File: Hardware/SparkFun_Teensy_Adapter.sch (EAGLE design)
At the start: 7 parts, among them J1 ARDUINO_R3_SHIELD, J2 AVR_SPI_PRG_6PTH

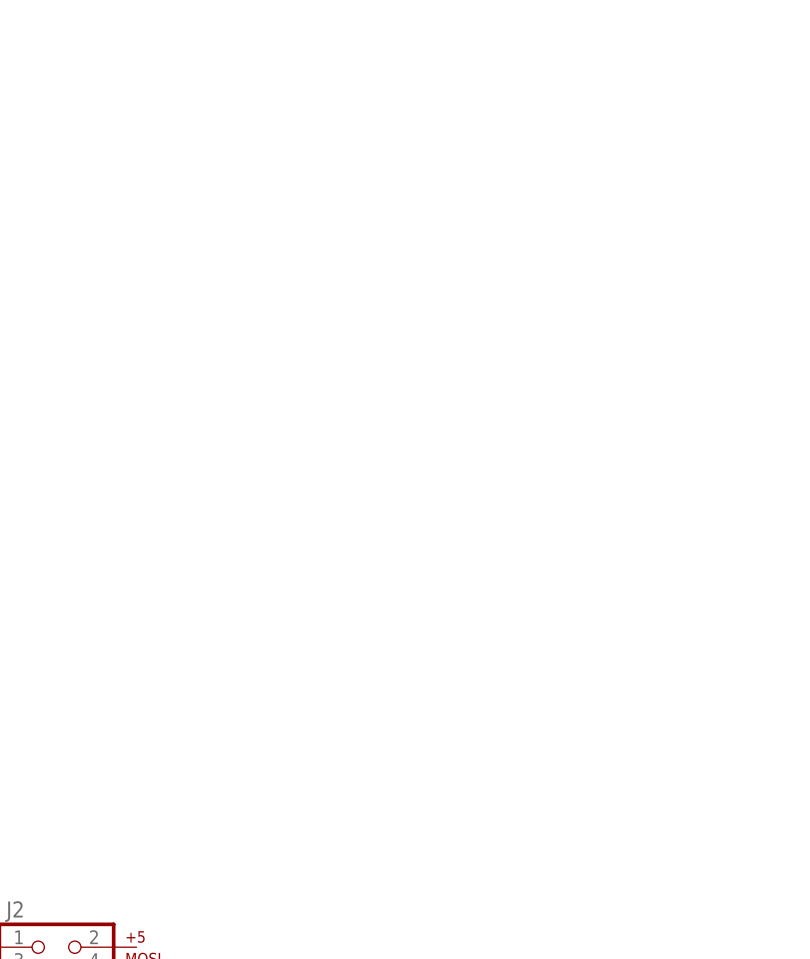
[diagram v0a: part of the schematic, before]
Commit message: Basic mechanical layout of board.
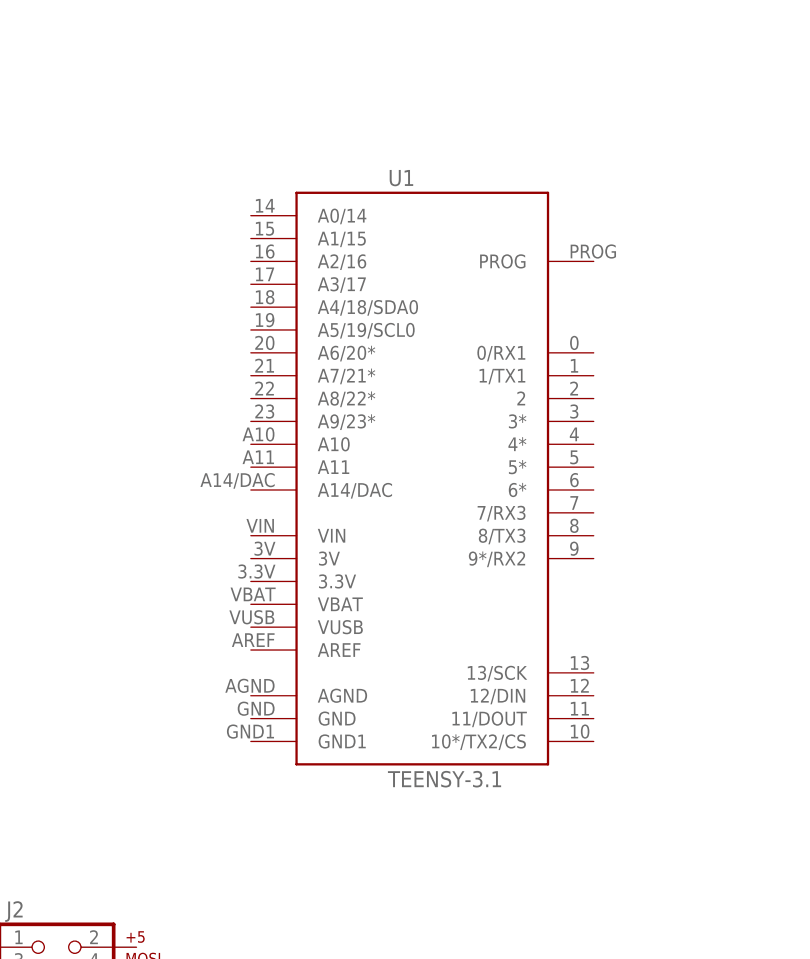
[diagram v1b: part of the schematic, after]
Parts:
- added U1: TEENSY-3.1, Testing:TEENSY-3.1
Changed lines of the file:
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@@
 <layer number="251" name="SMDround" color="12" fill="11" visible="no" active="no"/>
 <layer number="254" name="cooling" color="7" fill="1" visible="yes" active="yes"/>
+<layer number="255" name="routoute" color="7" fill="1" visible="yes" active="yes"/>
 </layers>
 <schematic xreflabel="%F%N/%S" xrefpart="/%S.%C%R">
@@
 <part name="J1" library="SparkFun-Boards" deviceset="ARDUINO_R3_SHIELD" device=""/>
 <part name="J2" library="SparkFun-Connectors" deviceset="AVR_SPI_PRG_6" device="PTH"/>
+<part name="U1" library="Testing" deviceset="TEENSY-3.1" device=""/>
 </parts>
 <sheets>
@@
 <instance part="J1" gate="G$1" x="88.9" y="109.22"/>
 <instance part="J2" gate="G$1" x="127" y="66.04"/>
+<instance part="U1" gate="G$1" x="154.94" y="88.9"/>
 </instances>
 <busses>

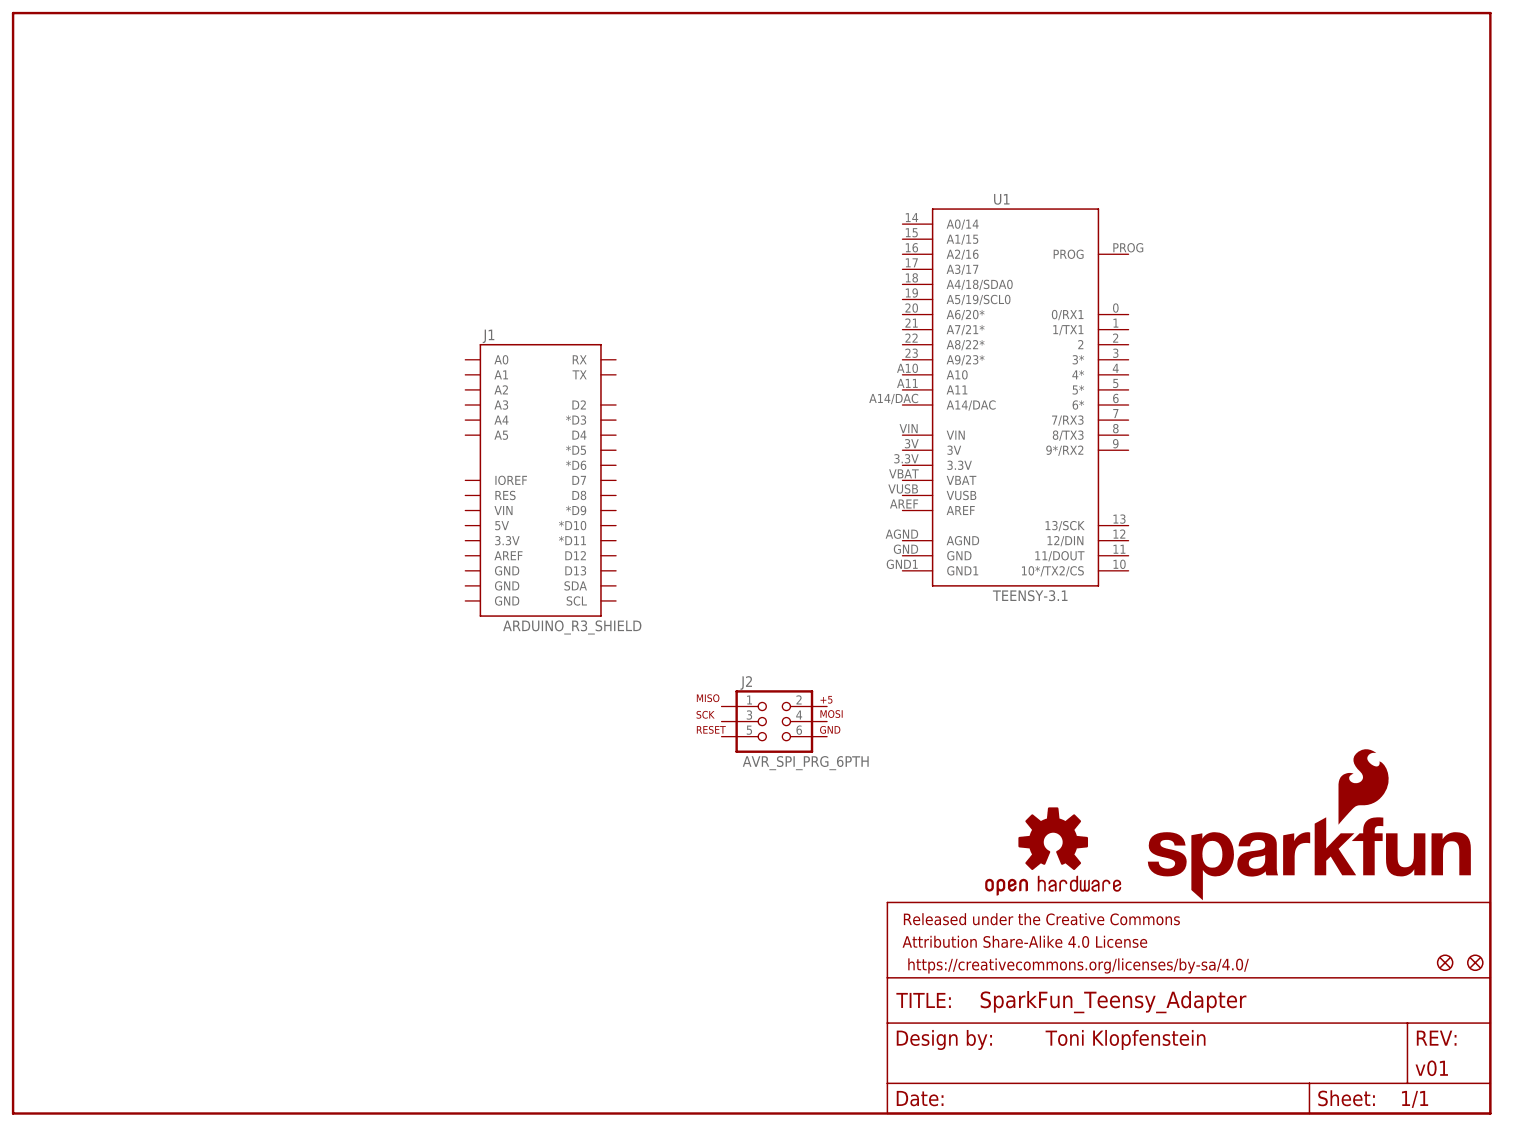
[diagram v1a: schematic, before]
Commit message: Power connectors added
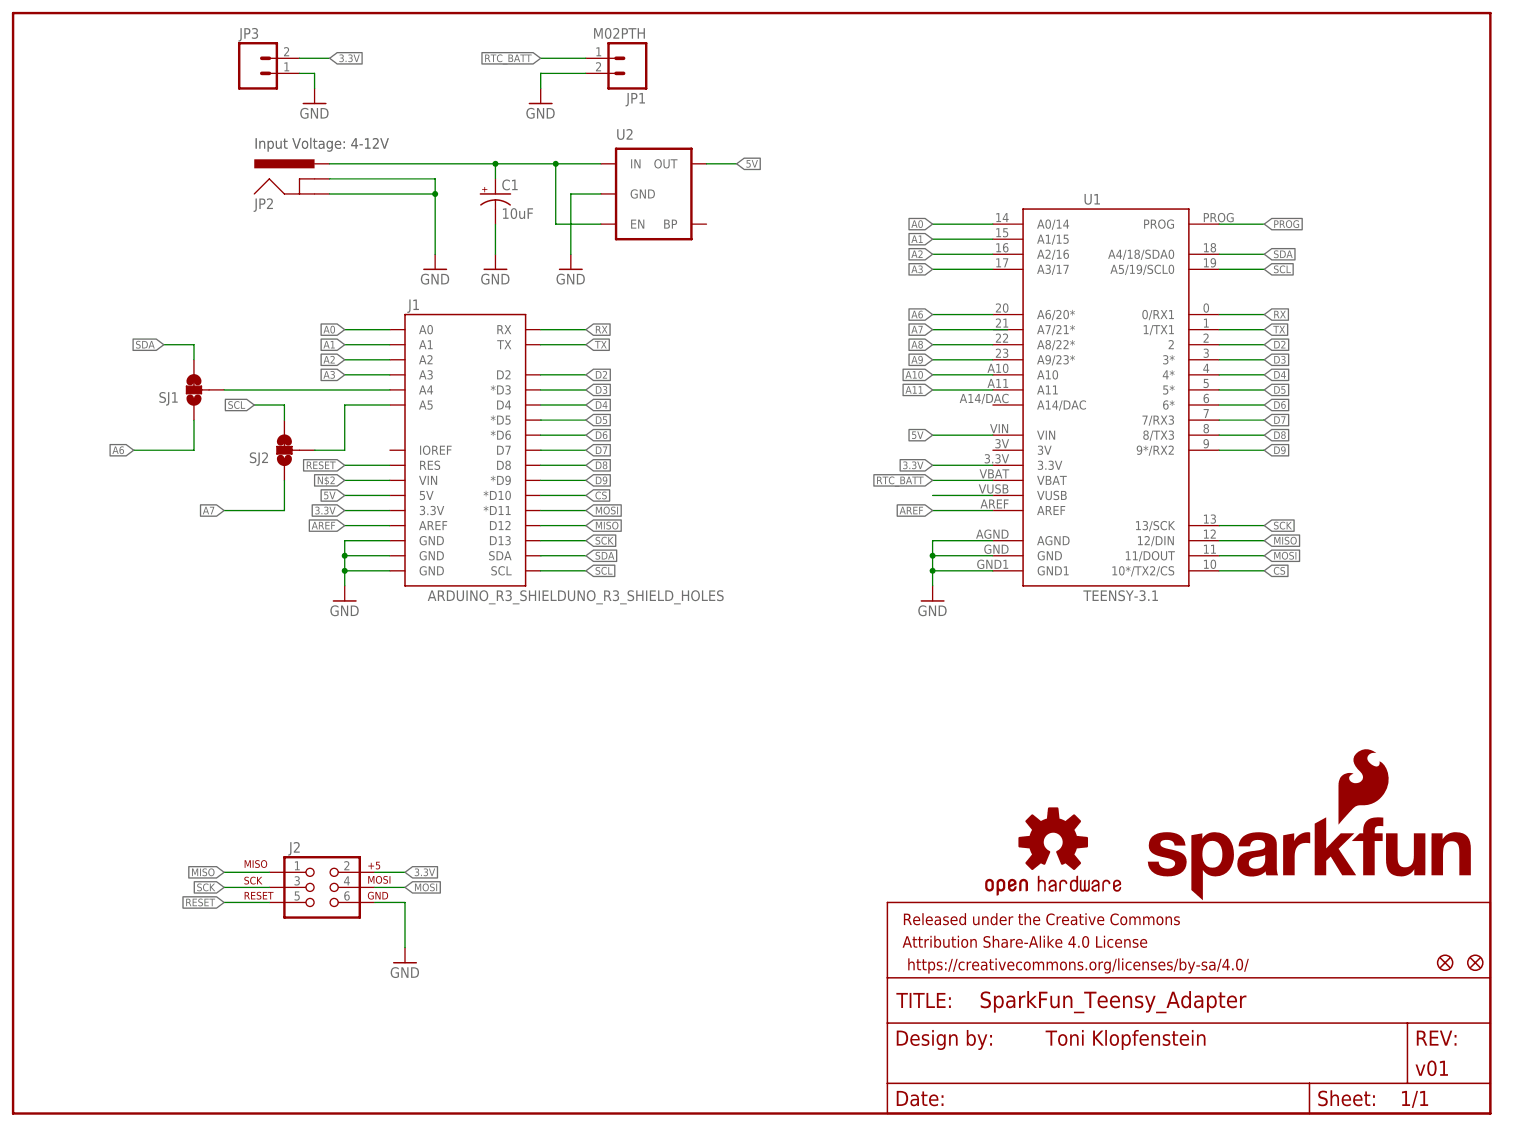
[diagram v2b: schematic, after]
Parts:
- added C1: 10uF, SparkFun-Capacitors:10UF-16V-10%(TANT)
- added JP1: M02PTH, SparkFun-Connectors:M02PTH
- added JP2: POWER_JACKPTH_LOCK, SparkFun-Connectors:POWER_JACKPTH_LOCK
- added JP3: M02JST-PTH-2, SparkFun-Connectors:M02JST-PTH-2
- added SJ1, SJ2: JUMPER-PAD-3-2OF3_NC_BY_TRACE_SMALL, SparkFun-Passives:JUMPER-PAD-3-2OF3_NC_BY_TRACE_SMALL
- added U2: (no value), SparkFun-PowerIC:MIC52055V
- J1: value ARDUINO_R3_SHIELD -> ARDUINO_R3_SHIELDUNO_R3_SHIELD_HOLES; device SparkFun-Boards:ARDUINO_R3_SHIELD -> Testing:ARDUINO_R3_SHIELDUNO_R3_SHIELD_HOLES
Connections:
- new net 3.3V: J1.3.3V, J2.2, JP3.2, U1.3.3V
- new net 5V: J1.5V, U1.VIN, U2.OUT
- new net A0: J1.A0, U1.A0/14
- new net A1: J1.A1, U1.A1/15
- new net A10: U1.A10
- new net A11: U1.A11
- new net A2: J1.A2, U1.A2/16
- new net A3: J1.A3, U1.A3/17
- new net A4: J1.A4, SJ1.2
- new net A5: J1.A5, SJ2.2
- new net A6: SJ1.1, U1.A6/20*
- new net A7: SJ2.1
- new net A8: U1.A8/22*
- new net A9: U1.A9/23*
- new net AREF: J1.AREF, U1.AREF
- new net CS: J1.*D10, U1.10*/TX2/CS
- new net D2: J1.D2, U1.2
- new net D3: J1.*D3, U1.3*
- new net D4: J1.D4, U1.4*
- new net D5: J1.*D5, U1.5*
- new net D6: J1.*D6, U1.6*
- new net D7: J1.D7, U1.7/RX3
- new net D8: J1.D8, U1.8/TX3
- new net D9: J1.*D9, U1.9*/RX2
- new net GND: C1.-, J1.GND@0, J1.GND@1, J1.GND@2, J2.6, JP1.2, JP2.GND, JP2.GNDBREAK, JP3.1, U1.AGND, U1.GND, U1.GND1, U2.GND
- new net MISO: J1.D12, J2.1, U1.12/DIN
- new net MOSI: J1.*D11, J2.4, U1.11/DOUT
- new net N$2: J1.VIN
- new net N$6: U1.VUSB
- new net PROG: U1.PROG
- new net RESET: J1.RES, J2.5
- new net RTC_BATT: JP1.1, U1.VBAT
- new net RX: J1.RX, U1.0/RX1
- new net SCK: J1.D13, J2.3, U1.13/SCK
- new net SCL: J1.SCL, SJ2.3, U1.A5/19/SCL0
- new net SDA: J1.SDA, SJ1.3, U1.A4/18/SDA0
- new net TX: J1.TX, U1.1/TX1
- new net VRAW: C1.+, JP2.PWR, U2.EN, U2.IN
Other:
- note added: "Input Voltage: 4-12V"
- moved on the sheet: J1, J2, U1

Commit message: Partial routing
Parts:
- added C2: (no value), SparkFun-Capacitors:CAP_POL7343
- added JP4: (no value), SparkFun-Connectors:M08
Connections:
- removed net N$6: U1.VUSB
- new net A14/DAC: JP4.2, U1.A14/DAC
- new net HV_AREF: J1.AREF
- new net N$9: JP4.1
- new net VUSB: C2.+, JP4.7, U1.VUSB
- net A10: now also JP4.4
- net A11: now also JP4.3
- net A8: now also JP4.6
- net A9: now also JP4.5
- net AREF: no longer J1.AREF
- net GND: now also C2.-
- net PROG: now also JP4.8
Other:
- note added: "5V"
- note added: "Add 100uF Cap for USB Host applications."
- note added: "Add 32.768kHZ crystal to Teensy for use of RTC."
- note added: "Cut trace between VUSB and VIN pads on Teensy to use external power supply."
- note added: "DNP"
- moved on the sheet: JP1
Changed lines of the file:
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@@
 <part name="C1" library="SparkFun-Capacitors" deviceset="10UF-16V-10%(TANT)" device="" value="10uF"/>
 <part name="GND8" library="SparkFun-Aesthetics" deviceset="GND" device=""/>
+<part name="C2" library="SparkFun-Capacitors" deviceset="CAP_POL" device="7343"/>
+<part name="GND9" library="SparkFun-Aesthetics" deviceset="GND" device=""/>
+<part name="JP4" library="SparkFun-Connectors" deviceset="M08" device=""/>
 </parts>
 <sheets>
@@
 <plain>
 <text x="40.64" y="162.56" size="1.778" layer="97">Input Voltage: 4-12V</text>
+<text x="106.68" y="144.78" size="1.778" layer="97">5V</text>
+<text x="193.04" y="170.18" size="1.778" layer="97">DNP</text>
+<text x="200.66" y="172.72" size="1.27" layer="97">Add 100uF Cap for USB Host applications. </text>
+<text x="149.86" y="160.02" size="1.27" layer="97">Add 32.768kHZ crystal to Teensy for use of RTC.  </text>
+<text x="33.02" y="147.32" size="1.27" layer="97">Cut trace between VUSB and VIN pads
+ on Teensy to use external power supply. </text>
 </plain>
 <instances>
@@
 <attribute name="NAME" x="43.18" y="111.379" size="1.778" layer="95" rot="R180"/>
 </instance>
-<instance part="JP1" gate="G$1" x="104.14" y="177.8" rot="R180"/>
-<instance part="GND4" gate="1" x="88.9" y="170.18"/>
+<instance part="JP1" gate="G$1" x="172.72" y="175.26" rot="R180"/>
+<instance part="GND4" gate="1" x="160.02" y="165.1"/>
 <instance part="JP2" gate="G$1" x="50.8" y="152.4" smashed="yes">
 <attribute name="NAME" x="40.64" y="152.4" size="1.778" layer="95"/>
@@
 <instance part="C1" gate="G$1" x="81.28" y="154.94"/>
 <instance part="GND8" gate="1" x="81.28" y="142.24"/>
+<instance part="C2" gate="G$1" x="190.5" y="175.26"/>
+<instance part="GND9" gate="1" x="190.5" y="165.1"/>
+<instance part="JP4" gate="G$1" x="101.6" y="38.1"/>
 </instances>
 <busses>
@@
 <segment>
 <pinref part="JP1" gate="G$1" pin="2"/>
-<wire x1="96.52" y1="175.26" x2="88.9" y2="175.26" width="0.1524" layer="91"/>
-<wire x1="88.9" y1="175.26" x2="88.9" y2="172.72" width="0.1524" layer="91"/>
+<wire x1="165.1" y1="172.72" x2="160.02" y2="172.72" width="0.1524" layer="91"/>
+<wire x1="160.02" y1="172.72" x2="160.02" y2="167.64" width="0.1524" layer="91"/>
 <pinref part="GND4" gate="1" pin="GND"/>
 </segment>
@@
 <wire x1="81.28" y1="149.86" x2="81.28" y2="144.78" width="0.1524" layer="91"/>
 </segment>
+<segment>
+<pinref part="C2" gate="G$1" pin="-"/>
+<wire x1="190.5" y1="170.18" x2="190.5" y2="167.64" width="0.1524" layer="91"/>
+<pinref part="GND9" gate="1" pin="GND"/>
+</segment>
 </net>
 <net name="RX" class="0">
@@
 <label x="154.94" y="124.46" size="1.27" layer="95" rot="R180" xref="yes"/>
 </segment>
+<segment>
+<pinref part="JP4" gate="G$1" pin="4"/>
+<wire x1="106.68" y1="38.1" x2="114.3" y2="38.1" width="0.1524" layer="91"/>
+<label x="114.3" y="38.1" size="1.27" layer="95" xref="yes"/>
+</segment>
 </net>
 <net name="A11" class="0">
@@
 <wire x1="165.1" y1="121.92" x2="154.94" y2="121.92" width="0.1524" layer="91"/>
 <label x="154.94" y="121.92" size="1.27" layer="95" rot="R180" xref="yes"/>
+</segment>
+<segment>
+<pinref part="JP4" gate="G$1" pin="3"/>
+<wire x1="106.68" y1="35.56" x2="114.3" y2="35.56" width="0.1524" layer="91"/>
+<label x="114.3" y="35.56" size="1.27" layer="95" xref="yes"/>
 </segment>
 </net>
@@
 <net name="AREF" class="0">
 <segment>
-<pinref part="J1" gate="G$1" pin="AREF"/>
-<wire x1="63.5" y1="99.06" x2="55.88" y2="99.06" width="0.1524" layer="91"/>
-<label x="55.88" y="99.06" size="1.27" layer="95" rot="R180" xref="yes"/>
-</segment>
-<segment>
 <pinref part="U1" gate="G$1" pin="AREF"/>
 <wire x1="165.1" y1="101.6" x2="154.94" y2="101.6" width="0.1524" layer="91"/>
@@
 <segment>
 <pinref part="JP1" gate="G$1" pin="1"/>
-<wire x1="96.52" y1="177.8" x2="88.9" y2="177.8" width="0.1524" layer="91"/>
-<label x="88.9" y="177.8" size="1.27" layer="95" rot="R180" xref="yes"/>
+<wire x1="165.1" y1="175.26" x2="160.02" y2="175.26" width="0.1524" layer="91"/>
+<label x="160.02" y="175.26" size="1.27" layer="95" rot="R180" xref="yes"/>
 </segment>
 </net>
@@
 <label x="154.94" y="129.54" size="1.27" layer="95" rot="R180" xref="yes"/>
 </segment>
+<segment>
+<pinref part="JP4" gate="G$1" pin="6"/>
+<wire x1="106.68" y1="43.18" x2="114.3" y2="43.18" width="0.1524" layer="91"/>
+<label x="114.3" y="43.18" size="1.27" layer="95" xref="yes"/>
+</segment>
 </net>
 <net name="A9" class="0">
@@
 <label x="154.94" y="127" size="1.27" layer="95" rot="R180" xref="yes"/>
 </segment>
-</net>
-<net name="N$6" class="0">
+<segment>
+<pinref part="JP4" gate="G$1" pin="5"/>
+<wire x1="106.68" y1="40.64" x2="114.3" y2="40.64" width="0.1524" layer="91"/>
+<label x="114.3" y="40.64" size="1.27" layer="95" xref="yes"/>
+</segment>
+</net>
+<net name="VUSB" class="0">
 <segment>
 <pinref part="U1" gate="G$1" pin="VUSB"/>
 <wire x1="165.1" y1="104.14" x2="154.94" y2="104.14" width="0.1524" layer="91"/>
+<label x="154.94" y="104.14" size="1.27" layer="95" rot="R180" xref="yes"/>
+</segment>
+<segment>
+<pinref part="C2" gate="G$1" pin="+"/>
+<wire x1="190.5" y1="177.8" x2="190.5" y2="180.34" width="0.1524" layer="91"/>
+<wire x1="190.5" y1="180.34" x2="195.58" y2="180.34" width="0.1524" layer="91"/>
+<label x="195.58" y="180.34" size="1.27" layer="95" xref="yes"/>
+</segment>
+<segment>
+<pinref part="JP4" gate="G$1" pin="7"/>
+<wire x1="106.68" y1="45.72" x2="114.3" y2="45.72" width="0.1524" layer="91"/>
+<label x="114.3" y="45.72" size="1.27" layer="95" xref="yes"/>
 </segment>
 </net>
@@
 <wire x1="203.2" y1="149.86" x2="210.82" y2="149.86" width="0.1524" layer="91"/>
 <label x="210.82" y="149.86" size="1.27" layer="95" xref="yes"/>
+</segment>
+<segment>
+<pinref part="JP4" gate="G$1" pin="8"/>
+<wire x1="106.68" y1="48.26" x2="114.3" y2="48.26" width="0.1524" layer="91"/>
+<label x="114.3" y="48.26" size="1.27" layer="95" xref="yes"/>
 </segment>
 </net>
@@
 <wire x1="167.64" y1="132.08" x2="154.94" y2="132.08" width="0.1524" layer="91"/>
 <label x="154.94" y="132.08" size="1.27" layer="95" rot="R180" xref="yes"/>
+</segment>
+</net>
+<net name="HV_AREF" class="0">
+<segment>
+<pinref part="J1" gate="G$1" pin="AREF"/>
+<wire x1="63.5" y1="99.06" x2="55.88" y2="99.06" width="0.1524" layer="91"/>
+<label x="55.88" y="99.06" size="1.27" layer="95" rot="R180" xref="yes"/>
+</segment>
+</net>
+<net name="A14/DAC" class="0">
+<segment>
+<pinref part="U1" gate="G$1" pin="A14/DAC"/>
+<wire x1="165.1" y1="119.38" x2="154.94" y2="119.38" width="0.1524" layer="91"/>
+<label x="154.94" y="119.38" size="1.27" layer="95" rot="R180" xref="yes"/>
+</segment>
+<segment>
+<pinref part="JP4" gate="G$1" pin="2"/>
+<wire x1="106.68" y1="33.02" x2="114.3" y2="33.02" width="0.1524" layer="91"/>
+<label x="114.3" y="33.02" size="1.27" layer="95" xref="yes"/>
+</segment>
+</net>
+<net name="N$9" class="0">
+<segment>
+<pinref part="JP4" gate="G$1" pin="1"/>
+<wire x1="106.68" y1="30.48" x2="114.3" y2="30.48" width="0.1524" layer="91"/>
+<label x="114.3" y="30.48" size="1.27" layer="95" xref="yes"/>
 </segment>
 </net>
@@
 </schematic>
 </drawing>
+<compatibility>
+<note version="6.3" minversion="6.2.2" severity="warning">
+Since Version 6.2.2 text objects can contain more than one line,
+which will not be processed correctly with this version.
+</note>
+</compatibility>
 </eagle>

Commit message: Routing finished
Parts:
- removed C2: (no value), SparkFun-Capacitors:CAP_POL7343
- removed JP1: M02PTH, SparkFun-Connectors:M02PTH
- removed JP4: (no value), SparkFun-Connectors:M08
- added JP6, JP7: M02PTH, SparkFun-Connectors:M02PTH
- added JP8: (no value), SparkFun-Connectors:M04PTH
- added JP9: (no value), SparkFun-Connectors:M03PTH
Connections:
- removed net N$9: JP4.1
- net A10: now also JP7.1; no longer JP4.4
- net A11: now also JP7.2; no longer JP4.3
- net A14/DAC: now also JP8.4; no longer JP4.2
- net A7: now also U1.A7/21*
- net A8: now also JP6.2; no longer JP4.6
- net A9: now also JP6.1; no longer JP4.5
- net AREF: now also JP9.3
- net GND: now also JP8.1, JP9.1; no longer C2.-, JP1.2
- net PROG: now also JP8.3; no longer JP4.8
- net RTC_BATT: now also JP8.2; no longer JP1.1
- net VUSB: now also JP9.2; no longer C2.+, JP4.7
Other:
- note added: "AREF/VBUS"
- note added: "Analog Breakouts"
- note added: "Arduino Footprint Connections"
- note added: "Jumpers default to SDA/SCL. Can be adjusted to A6/A7 for Leonardo-compatible shields."
- note added: "Power Connections"
- note added: "RTC Clock/ADC/PROG"
- note added: "SPI Header"
- note added: "Teensy 3.1 Connectors"
- note removed: "DNP"
- moved on the sheet: C1, J1, J2, JP2, JP3, SJ1, SJ2, U1, U2
